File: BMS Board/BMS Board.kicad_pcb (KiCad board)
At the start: 4 copper layers, 106.5 x 97 mm, 204 parts, among them J1 Conn_01x02, Q1 NMOS, U1 BQ76920PW, U10 TLV70033_SOT23-5, U2 TCA9548APWR, U3 BQ76920PW, U4 BQ76920PW, U5 BQ76920PW, U6 BQ76920PW, U7 BQ76920PW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

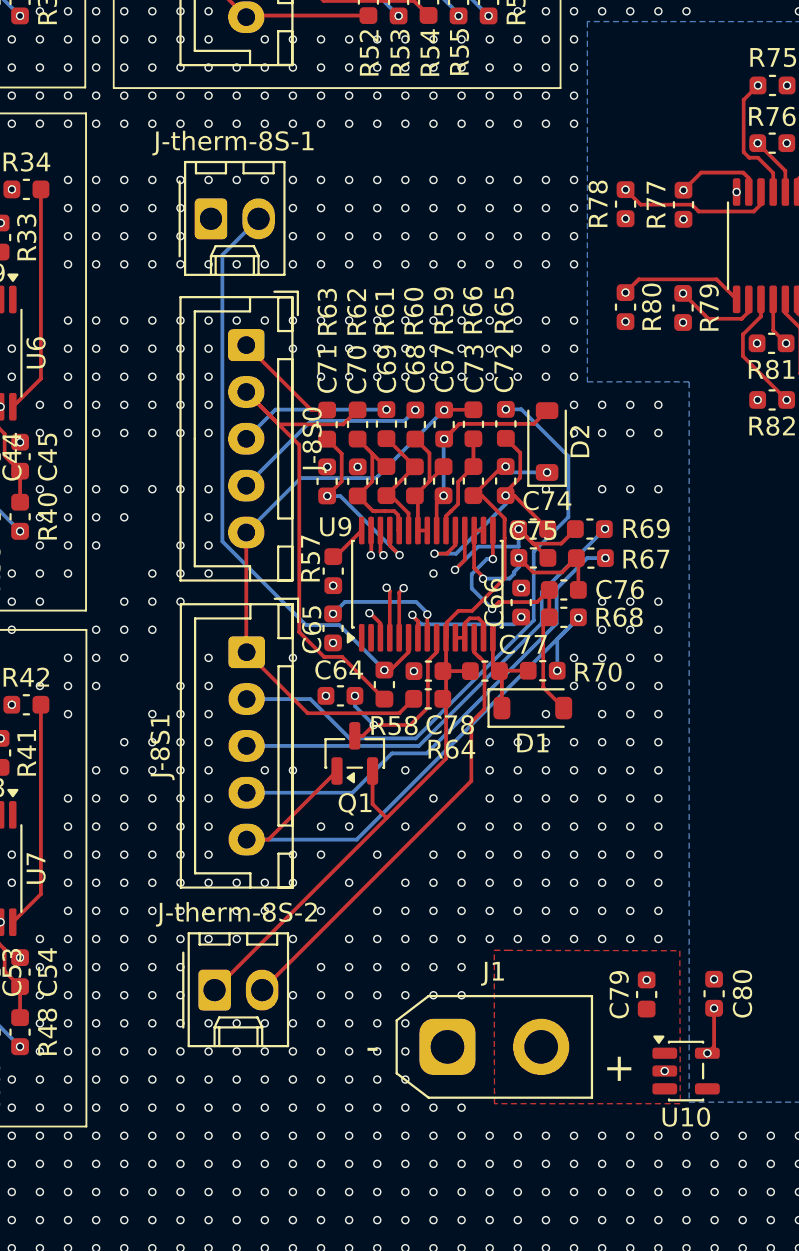
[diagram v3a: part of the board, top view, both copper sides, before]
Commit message: added LED to monitor 5v power
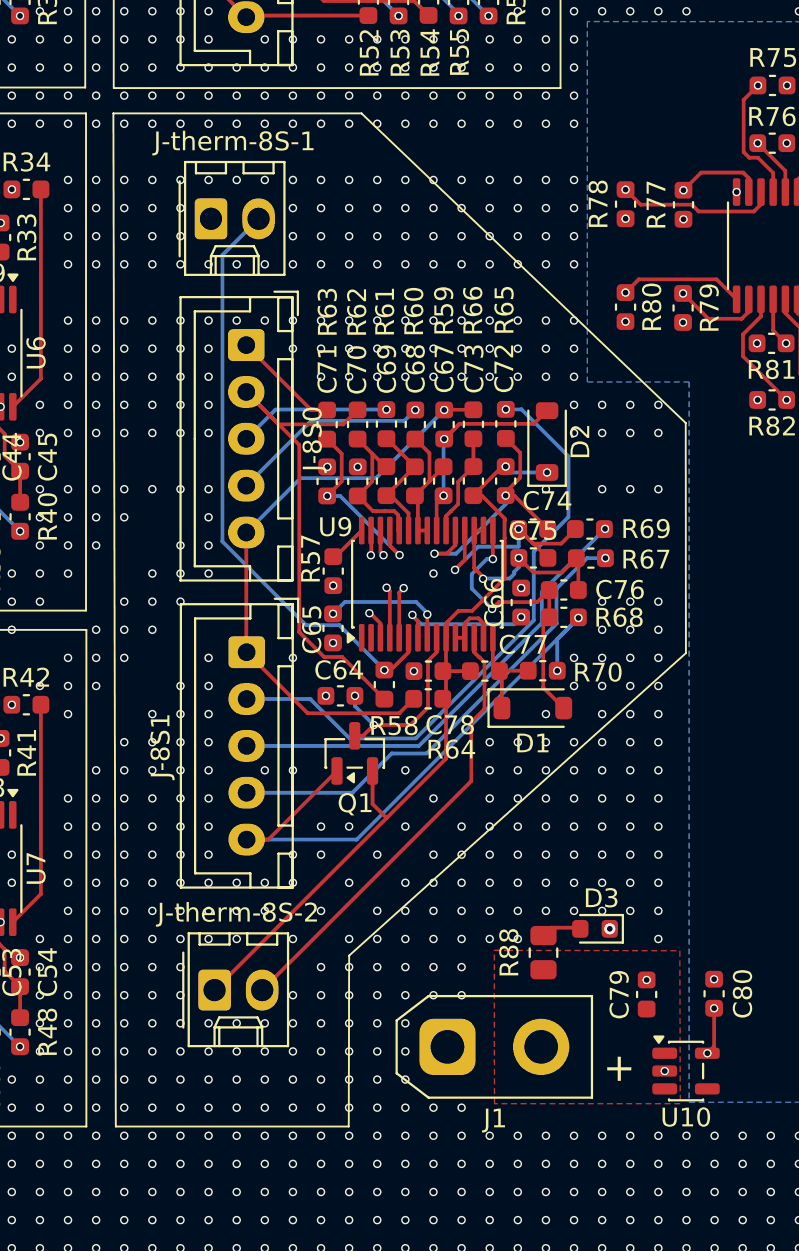
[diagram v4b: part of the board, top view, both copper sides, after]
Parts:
- added D3: LED, Diode_SMD:D_0603_1608Metric, F.Cu at (103.1, 108.7)
- added R88: 1k, Resistor_SMD:R_0805_2012Metric, F.Cu at (100.4, 109.9)
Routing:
- net Net-(D3-A): track 0.00 -> 2.16 mm
- net GND: vias 2825 -> 2822

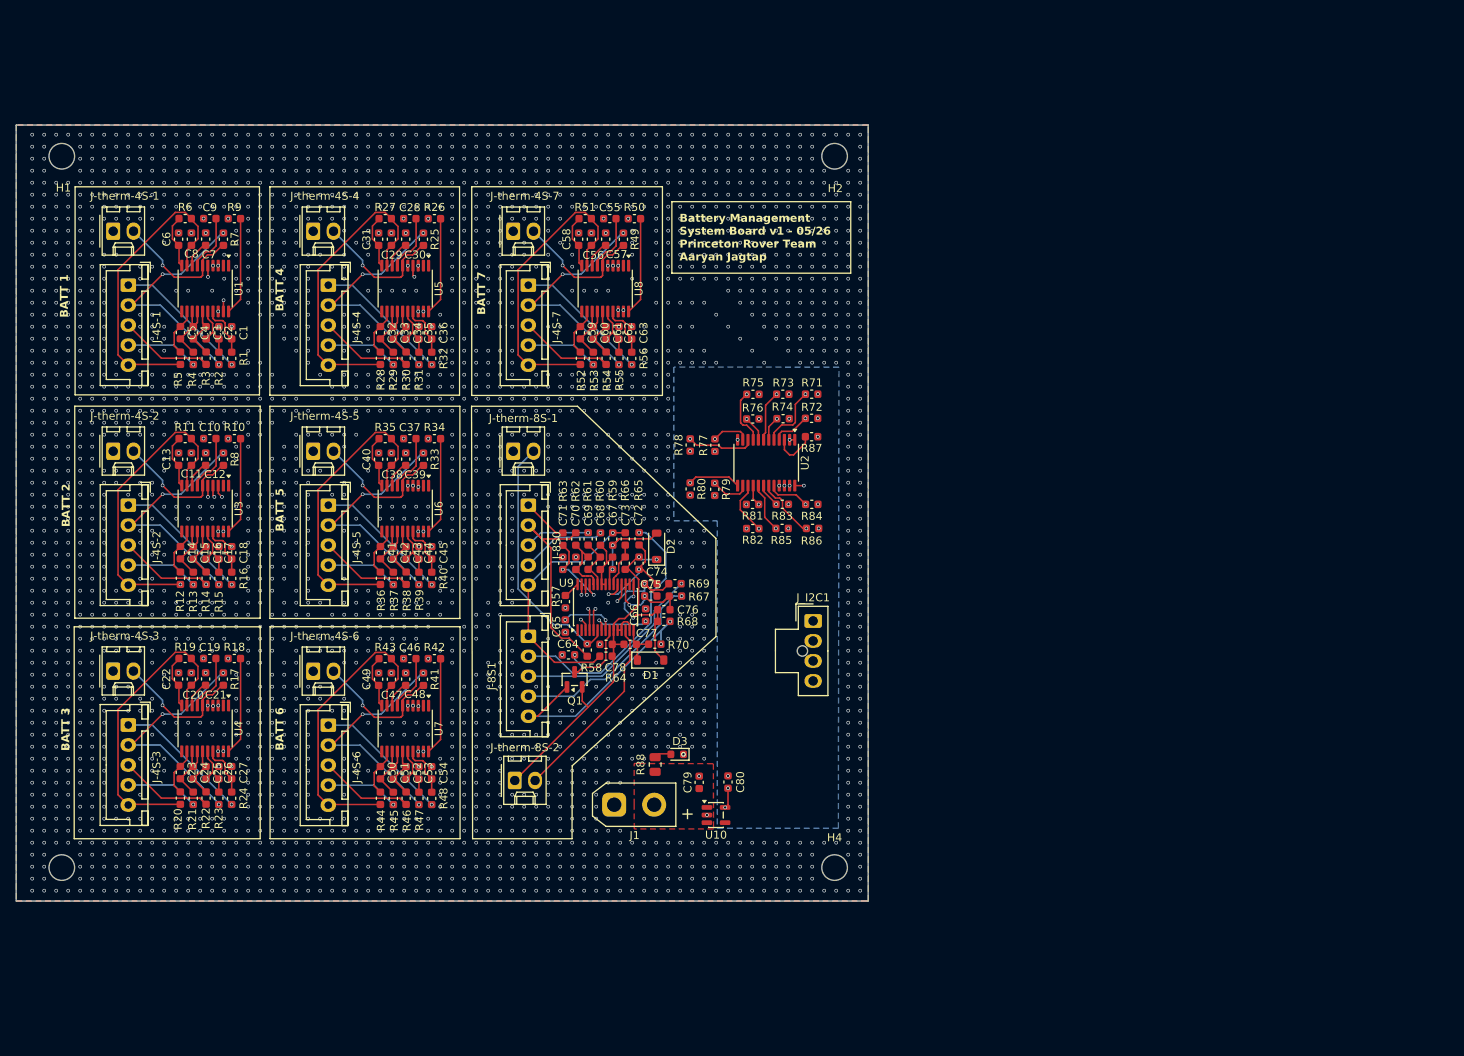
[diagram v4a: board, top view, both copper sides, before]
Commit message: added mounting holes
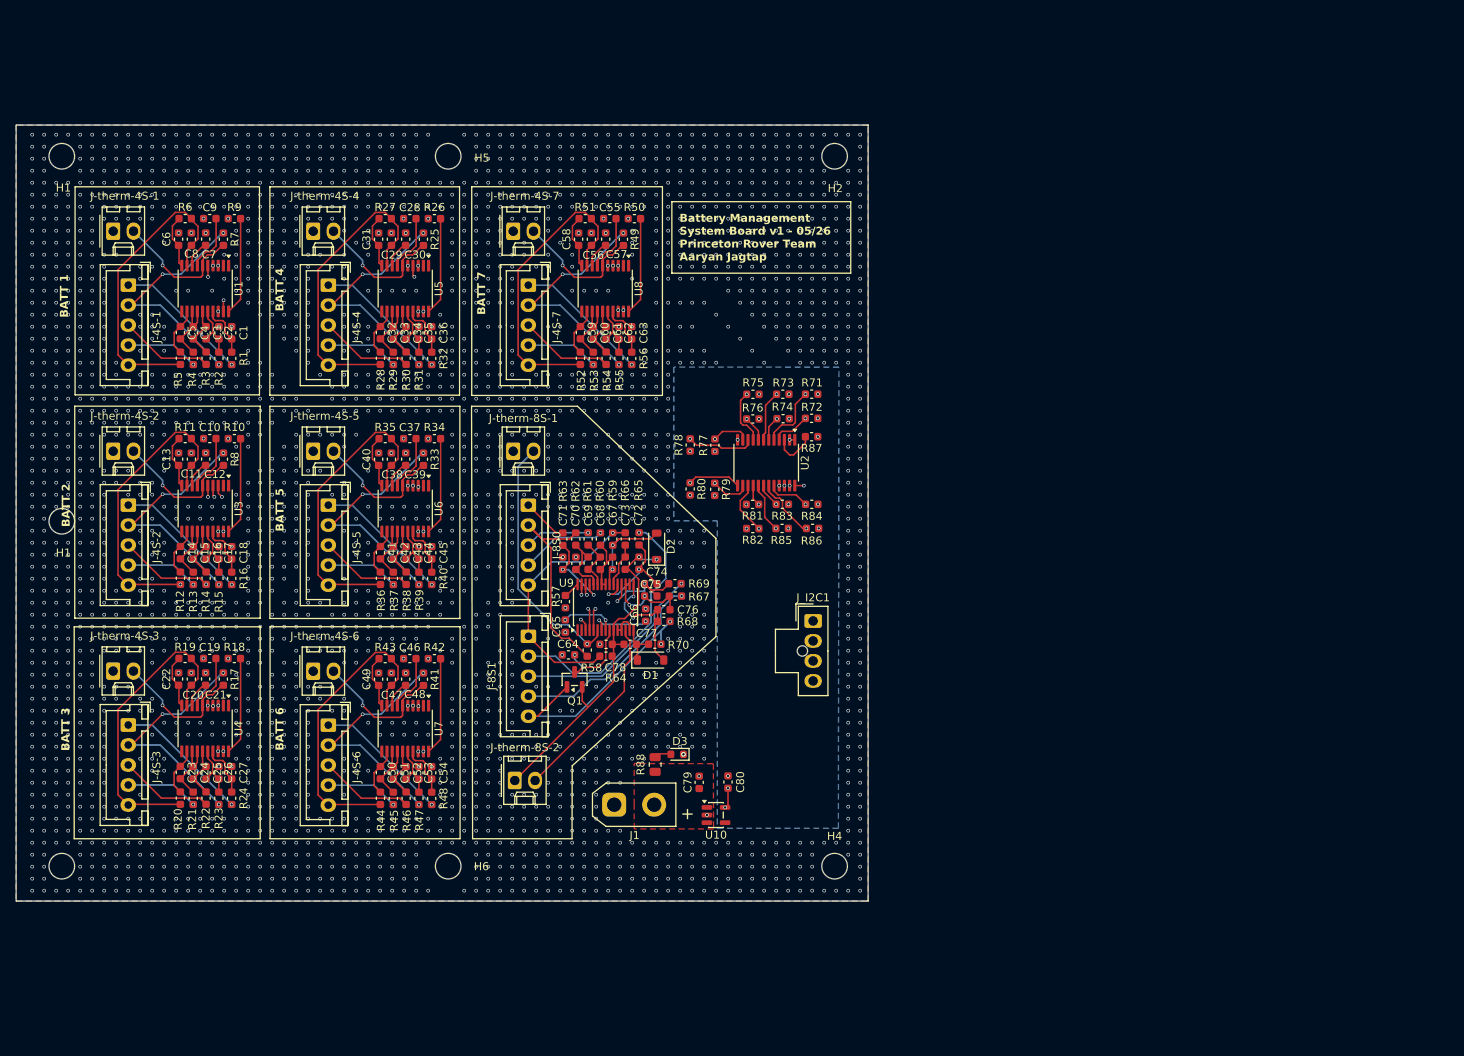
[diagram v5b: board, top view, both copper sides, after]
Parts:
- added H1: MountingHole, MountingHole:MountingHole_3.2mm_M3_DIN965, F.Cu at (26.2, 79.5)
- added H5: MountingHole, MountingHole:MountingHole_3.2mm_M3_DIN965, F.Cu at (74.5, 33.9)
- added H6: MountingHole, MountingHole:MountingHole_3.2mm_M3_DIN965, F.Cu at (74.5, 122.6)
- moved H3 0.18 mm to (26.2, 122.6)
- moved H4 0.18 mm to (122.8, 122.6)
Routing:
- net GND: vias 2822 -> 2794

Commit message: minor updates to BMS; edge cuts, GND pour, via stitching, missed connections for PDB
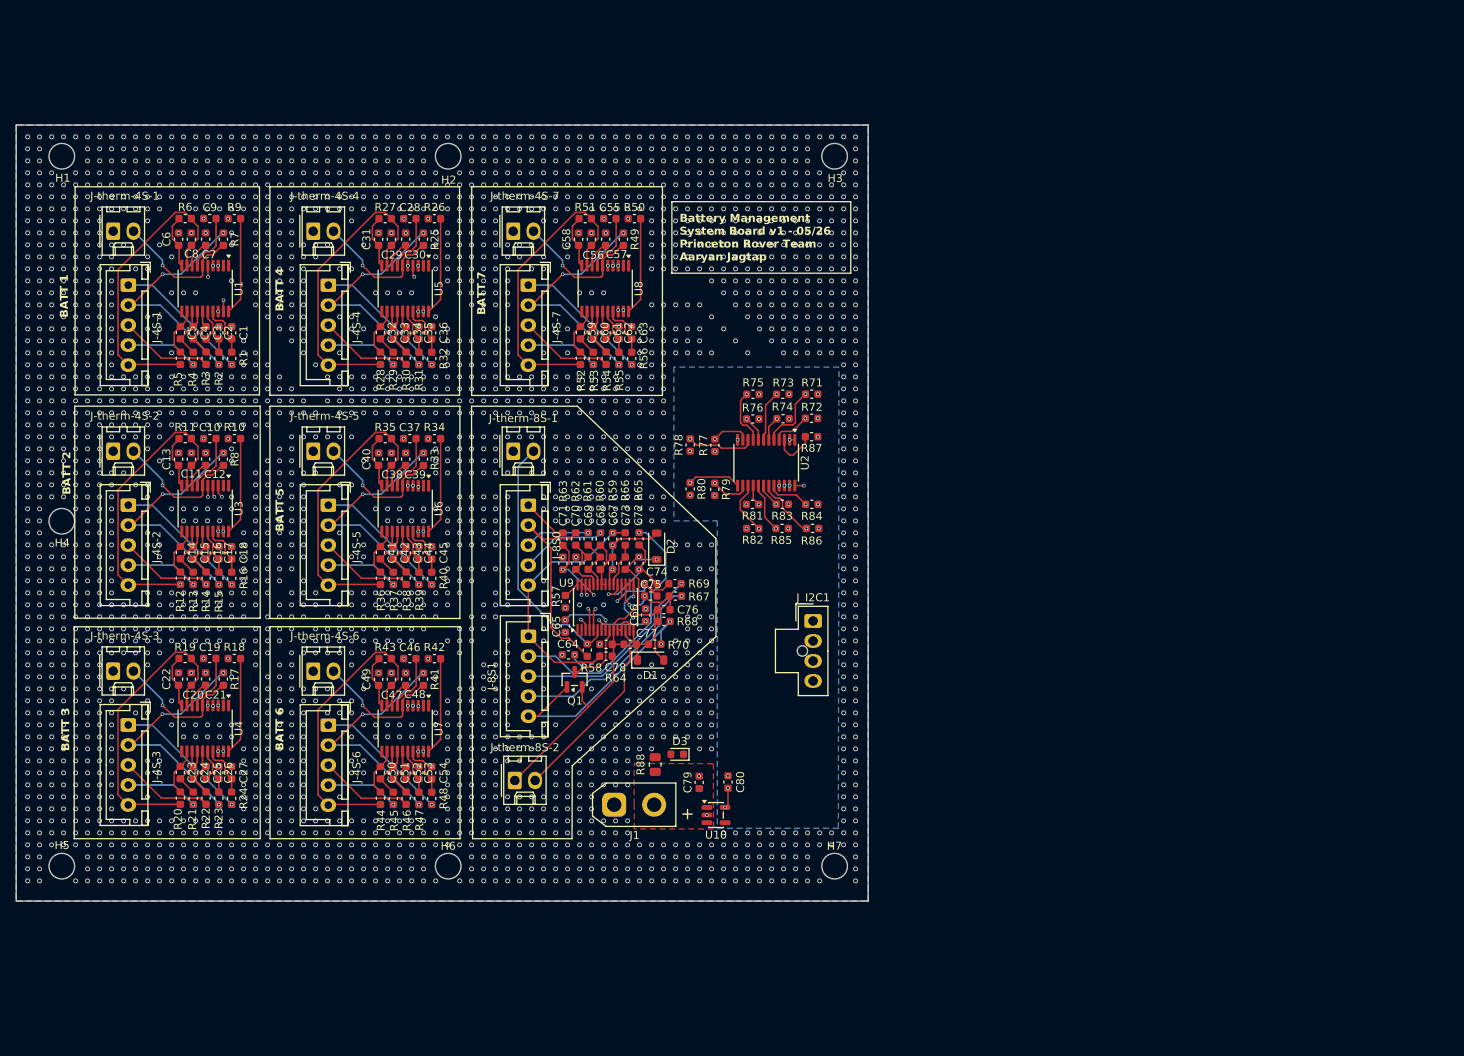
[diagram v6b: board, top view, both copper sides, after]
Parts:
- renumbered H5 to H2, H2 to H3, H1 to H4, H3 to H5, H4 to H7
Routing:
- net Net-(D3-A): track 2.16 -> 0.00 mm
- net GND: vias 2794 -> 2677
